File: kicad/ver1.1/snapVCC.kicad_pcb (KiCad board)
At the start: 2 copper layers, 25.9 x 17.3 mm, 25 parts, among them P1 CONN_01X03, P2 CONN_01X02, Q1 IRLML9301TRPbF, U1 TPS560200

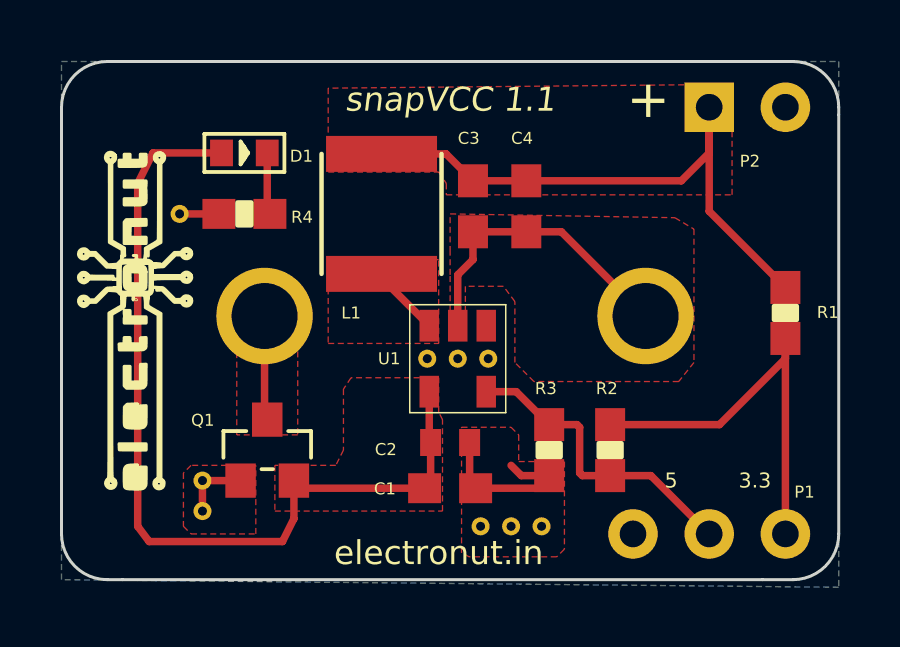
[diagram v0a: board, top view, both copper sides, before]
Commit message: fixed 0402 footprint issues
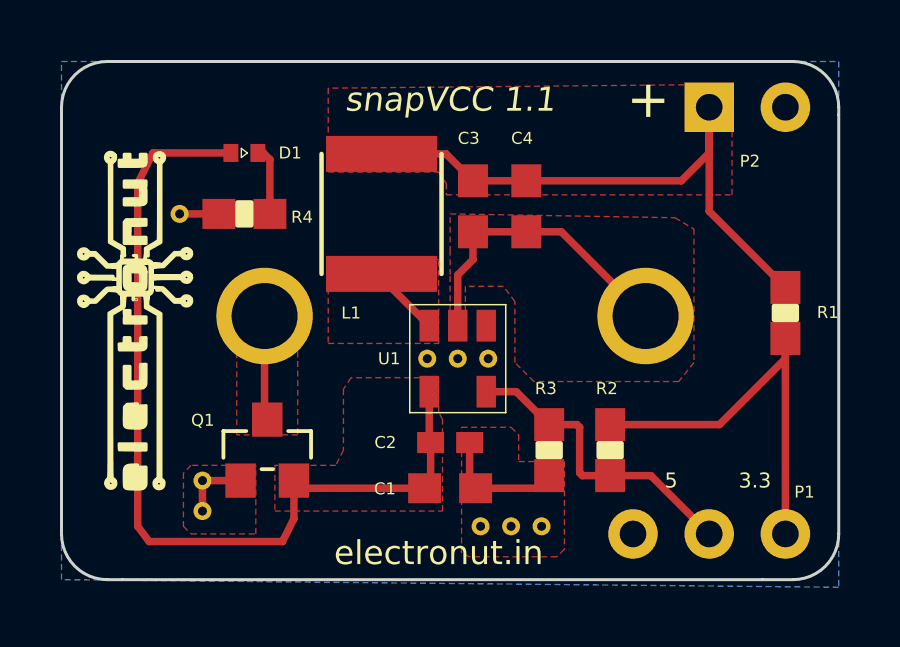
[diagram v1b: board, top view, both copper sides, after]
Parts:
- C2: footprint snapVCC_lib:0402-CAP -> snapVCC_lib:0402-seeed
- D1: footprint snapVCC_lib:LED-0603 -> snapVCC_lib:SML-P11_LED_0402
- U1: footprint SOT-23-5 -> snapVCC_lib:SOT-23-5
- turned D1 to 180 degrees
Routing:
- net GND: track 19.5 -> 18.1 mm
